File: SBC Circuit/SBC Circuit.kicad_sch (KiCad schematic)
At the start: 22 parts, among them J3 Conn_01x06_Pin, SW1 RESET, U1 MC68000FN, U11 MC34064P, U2 XC9572XL, X1 SG-531

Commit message: Wire phase done
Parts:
- added TP7: ~{BERR}, TestPoint:TestPoint_Keystone_5000-5004_Miniature, symbol Connector:TestPoint
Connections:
- net as: now also U2.28 (P28); no longer U2.22 (P22)
- net berr: now also U2.20 (P20), TP7.1; no longer U2.12 (P12)
- net dtack: now also U2.24 (P24); no longer U2.14 (P14)
- net fc0: now also U2.18 (P18); no longer U2.27 (P27)
- net fc1: now also U2.12 (P12); no longer U2.28 (P28)
- net fc2: now also U2.14 (P14); no longer U2.25 (P25)
- net ipl0: now also U2.13 (P13); no longer U2.26 (P26)
- net ipl1: now also U2.19 (P19); no longer U2.24 (P24)
- net ipl2: now also U2.22 (P22); no longer U2.13 (P13)
- net lds: now also U2.26 (P26); no longer U2.18 (P18)
- net rw: now also U2.25 (P25); no longer U2.19 (P19)
- net uds: now also U2.27 (P27); no longer U2.20 (P20)

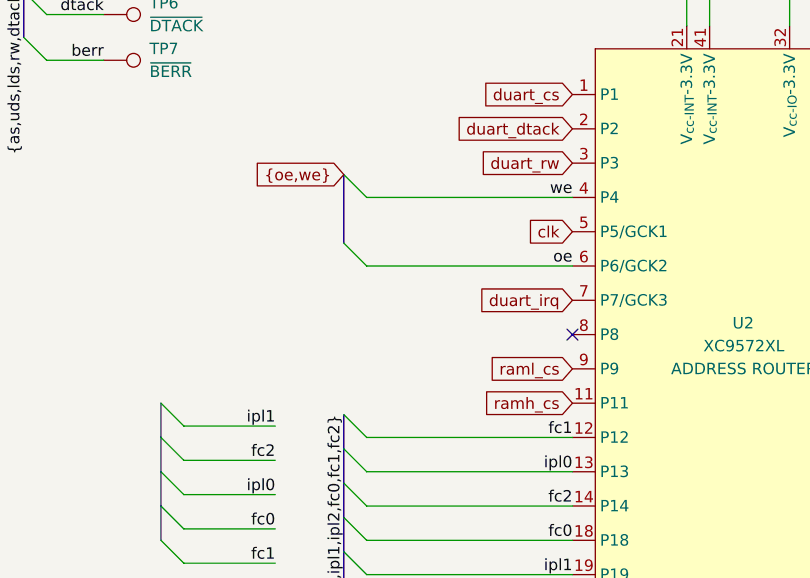
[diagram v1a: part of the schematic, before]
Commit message: Connect some power lines
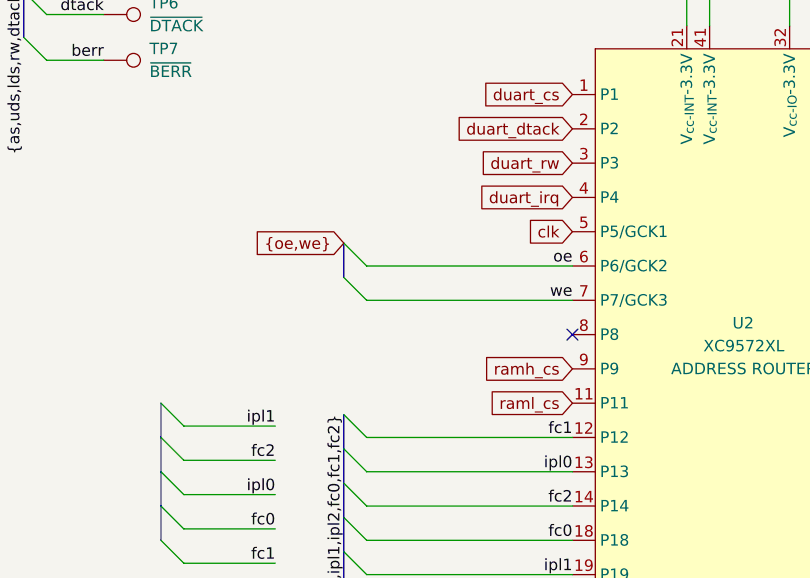
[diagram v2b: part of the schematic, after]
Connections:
- net duart_irq: now also U2.4 (P4); no longer U2.7 (P7/GCK3)
- net ramh_cs: now also U2.9 (P9); no longer U2.11 (P11)
- net raml_cs: now also U2.11 (P11); no longer U2.9 (P9)
- net we: now also U2.7 (P7/GCK3); no longer U2.4 (P4)
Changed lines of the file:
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@@
+    (stroke (width 0) (type default))
+  )
+  (bus_entry (at 58.42 128.27) (size 2.54 2.54)
     (stroke (width 0) (type default))
   )
@@
     (stroke (width 0) (type default))
   )
-  (bus_entry (at 58.42 120.65) (size 2.54 2.54)
+  (bus_entry (at 58.42 132.08) (size 2.54 2.54)
     (stroke (width 0) (type default))
   )
@@
     (stroke (width 0) (type default))
   )
-  (bus_entry (at 58.42 128.27) (size 2.54 2.54)
-    (stroke (width 0) (type default))
-  )
   (bus_entry (at 134.62 151.13) (size -2.54 2.54)
     (stroke (width 0) (type default))
@@
     (stroke (width 0) (type default))
   )
+  (wire (pts (xy 60.96 130.81) (xy 83.82 130.81))
+    (stroke (width 0) (type default))
+  )
   (wire (pts (xy 121.92 111.76) (xy 132.08 111.76))
     (stroke (width 0) (type default))
@@
     (stroke (width 0) (type default))
   )
+  (bus (pts (xy 58.42 128.27) (xy 58.42 132.08))
+    (stroke (width 0) (type default))
+  )
   (wire (pts (xy 106.68 55.88) (xy 106.68 50.8))
     (stroke (width 0) (type default))
@@
     (stroke (width 0) (type default))
   )
-  (wire (pts (xy 60.96 130.81) (xy 83.82 130.81))
-    (stroke (width 0) (type default))
-  )
   (wire (pts (xy 209.55 30.48) (xy 213.36 30.48))
     (stroke (width 0) (type default))
@@
     (stroke (width 0) (type default))
   )
-  (wire (pts (xy 60.96 123.19) (xy 83.82 123.19))
-    (stroke (width 0) (type default))
-  )
   (wire (pts (xy 93.98 38.1) (xy 93.98 41.91))
     (stroke (width 0) (type default))
@@
     (stroke (width 0) (type default))
   )
-  (bus (pts (xy 58.42 120.65) (xy 58.42 128.27))
-    (stroke (width 0) (type default))
-  )
   (bus (pts (xy 134.62 113.03) (xy 134.62 116.84))
     (stroke (width 0) (type default))
@@
   )
   (bus (pts (xy 264.16 53.34) (xy 264.16 55.88))
+    (stroke (width 0) (type default))
+  )
+  (wire (pts (xy 60.96 134.62) (xy 83.82 134.62))
     (stroke (width 0) (type default))
   )
@@
     (effects (font (size 1.27 1.27)) (justify left bottom))
   )
+  (label "fc1" (at 83.82 149.86 180)
+    (effects (font (size 1.27 1.27)) (justify right bottom))
+  )
+  (label "addr19" (at 251.46 96.52 0) (fields_autoplaced)
+    (effects (font (size 1.27 1.27)) (justify left bottom))
+  )
+  (label "fc1" (at 50.8 163.83 180) (fields_autoplaced)
+    (effects (font (size 1.27 1.27)) (justify right bottom))
+  )
+  (label "dtack" (at 200.66 77.47 180) (fields_autoplaced)
+    (effects (font (size 1.27 1.27)) (justify right bottom))
+  )
   (label "oe" (at 83.82 130.81 180) (fields_autoplaced)
-    (effects (font (size 1.27 1.27)) (justify right bottom))
-  )
-  (label "fc1" (at 83.82 149.86 180)
-    (effects (font (size 1.27 1.27)) (justify right bottom))
-  )
-  (label "addr19" (at 251.46 96.52 0) (fields_autoplaced)
-    (effects (font (size 1.27 1.27)) (justify left bottom))
-  )
-  (label "fc1" (at 50.8 163.83 180) (fields_autoplaced)
-    (effects (font (size 1.27 1.27)) (justify right bottom))
-  )
-  (label "dtack" (at 200.66 77.47 180) (fields_autoplaced)
     (effects (font (size 1.27 1.27)) (justify right bottom))
   )
@@
     (effects (font (size 1.27 1.27)) (justify left bottom))
   )
-  (label "we" (at 83.82 123.19 180) (fields_autoplaced)
-    (effects (font (size 1.27 1.27)) (justify right bottom))
-  )
   (label "{ipl0,ipl1,ipl2,fc0,fc1,fc2}" (at 187.96 91.44 180) (fields_autoplaced)
     (effects (font (size 1.27 1.27)) (justify right bottom))
@@
   (label "addr9" (at 251.46 71.12 0) (fields_autoplaced)
     (effects (font (size 1.27 1.27)) (justify left bottom))
+  )
+  (label "we" (at 83.82 134.62 180) (fields_autoplaced)
+    (effects (font (size 1.27 1.27)) (justify right bottom))
   )
   (label "data12" (at 251.46 139.7 0) (fields_autoplaced)
@@
     )
   )
-  (global_label "ramh_cs" (shape input) (at 83.82 146.05 180) (fields_autoplaced)
-    (effects (font (size 1.27 1.27)) (justify right))
-    (property "Intersheetrefs" "${INTERSHEET_REFS}" (at 72.973 146.05 0)
-      (effects (font (size 1.27 1.27)) (justify right) hide)
-    )
-    (property "Netclass" "signal" (at 83.82 148.2408 0)
-      (effects (font (size 1.27 1.27)) (justify right) hide)
-    )
-  )
-  (global_label "duart_irq" (shape input) (at 83.82 134.62 180) (fields_autoplaced)
-    (effects (font (size 1.27 1.27)) (justify right))
-    (property "Intersheetrefs" "${INTERSHEET_REFS}" (at 72.3683 134.62 0)
-      (effects (font (size 1.27 1.27)) (justify right) hide)
-    )
-    (property "Netclass" "signal" (at 83.82 136.8108 0)
-      (effects (font (size 1.27 1.27)) (justify right) hide)
-    )
-  )
-  (global_label "raml_cs" (shape input) (at 83.82 142.24 180) (fields_autoplaced)
-    (effects (font (size 1.27 1.27)) (justify right))
-    (property "Intersheetrefs" "${INTERSHEET_REFS}" (at 73.4568 142.24 0)
-      (effects (font (size 1.27 1.27)) (justify right) hide)
-    )
-    (property "Netclass" "signal" (at 83.82 144.4308 0)
-      (effects (font (size 1.27 1.27)) (justify right) hide)
-    )
-  )
   (global_label "clk" (shape input) (at 83.82 127 180) (fields_autoplaced)
     (effects (font (size 1.27 1.27)) (justify right))
@@
     )
   )
-  (global_label "{oe,we}" (shape input) (at 58.42 120.65 180) (fields_autoplaced)
+  (global_label "ramh_cs" (shape input) (at 83.82 142.24 180) (fields_autoplaced)
     (effects (font (size 1.27 1.27)) (justify right))
-    (property "Intersheetrefs" "${INTERSHEET_REFS}" (at 48.4799 120.65 0)
-      (effects (font (size 1.27 1.27)) (justify right) hide)
-    )
-    (property "Netclass" "bus" (at 58.42 122.8408 0)
+    (property "Intersheetrefs" "${INTERSHEET_REFS}" (at 72.973 142.24 0)
+      (effects (font (size 1.27 1.27)) (justify right) hide)
+    )
+    (property "Netclass" "signal" (at 83.82 144.4308 0)
+      (effects (font (size 1.27 1.27)) (justify right) hide)
+    )
+  )
+  (global_label "duart_irq" (shape input) (at 83.82 123.19 180) (fields_autoplaced)
+    (effects (font (size 1.27 1.27)) (justify right))
+    (property "Intersheetrefs" "${INTERSHEET_REFS}" (at 72.3683 123.19 0)
+      (effects (font (size 1.27 1.27)) (justify right) hide)
+    )
+    (property "Netclass" "signal" (at 83.82 125.3808 0)
+      (effects (font (size 1.27 1.27)) (justify right) hide)
+    )
+  )
+  (global_label "raml_cs" (shape input) (at 83.82 146.05 180) (fields_autoplaced)
+    (effects (font (size 1.27 1.27)) (justify right))
+    (property "Intersheetrefs" "${INTERSHEET_REFS}" (at 73.4568 146.05 0)
+      (effects (font (size 1.27 1.27)) (justify right) hide)
+    )
+    (property "Netclass" "signal" (at 83.82 148.2408 0)
       (effects (font (size 1.27 1.27)) (justify right) hide)
     )
@@
       (effects (font (size 1.27 1.27)) (justify right) hide)
     )
+  )
+  (global_label "{oe,we}" (shape input) (at 58.42 128.27 180) (fields_autoplaced)
+    (effects (font (size 1.27 1.27)) (justify right))
+    (property "Intersheetrefs" "${INTERSHEET_REFS}" (at 48.4799 128.27 0)
+      (effects (font (size 1.27 1.27)) (justify right) hide)
+    )
+    (property "Netclass" "bus" (at 58.42 130.4608 0)
+      (effects (font (size 1.27 1.27)) (justify right) hide)
+    )

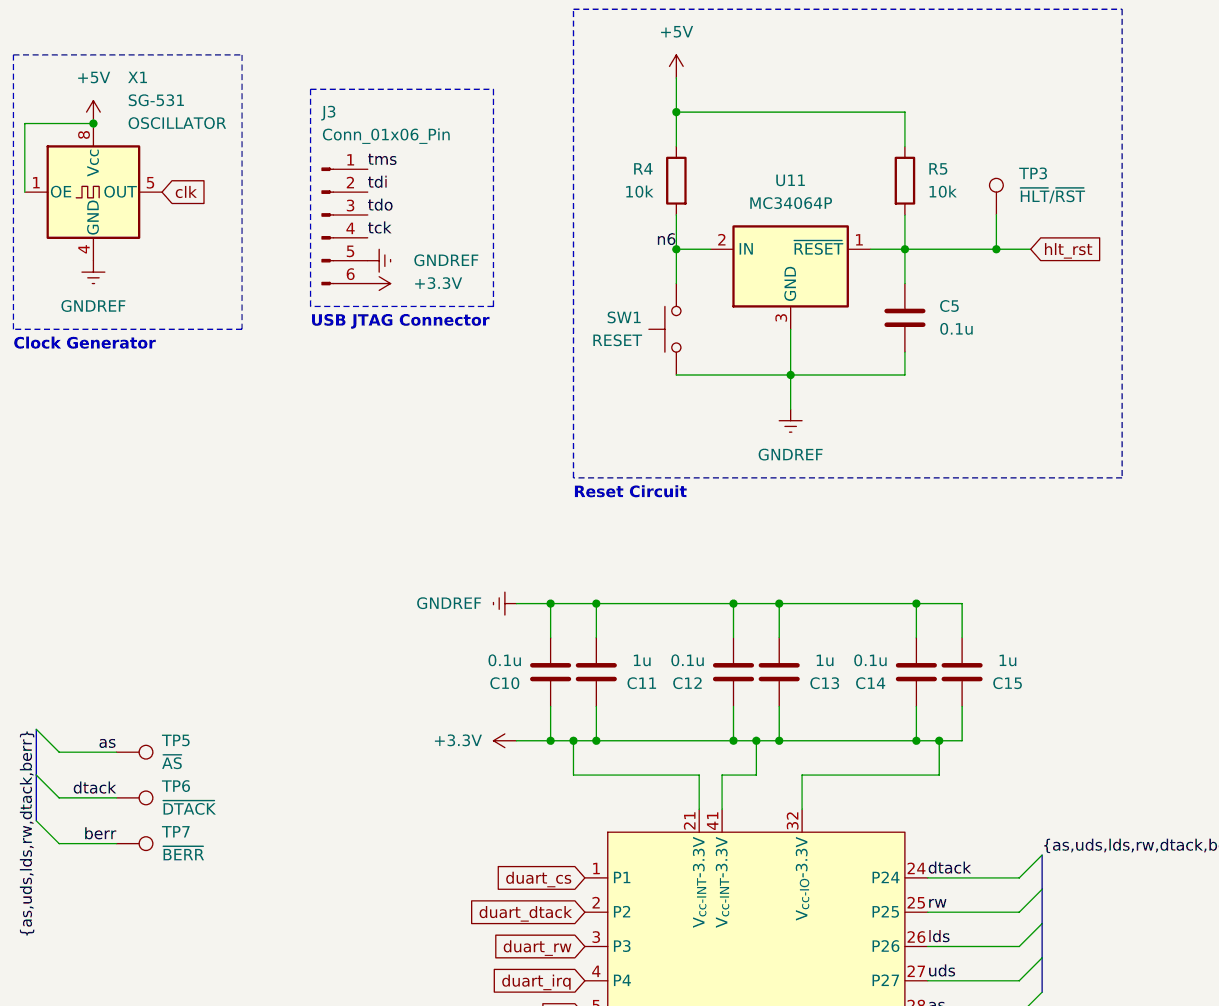
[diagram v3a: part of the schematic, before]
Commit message: Add ground test point
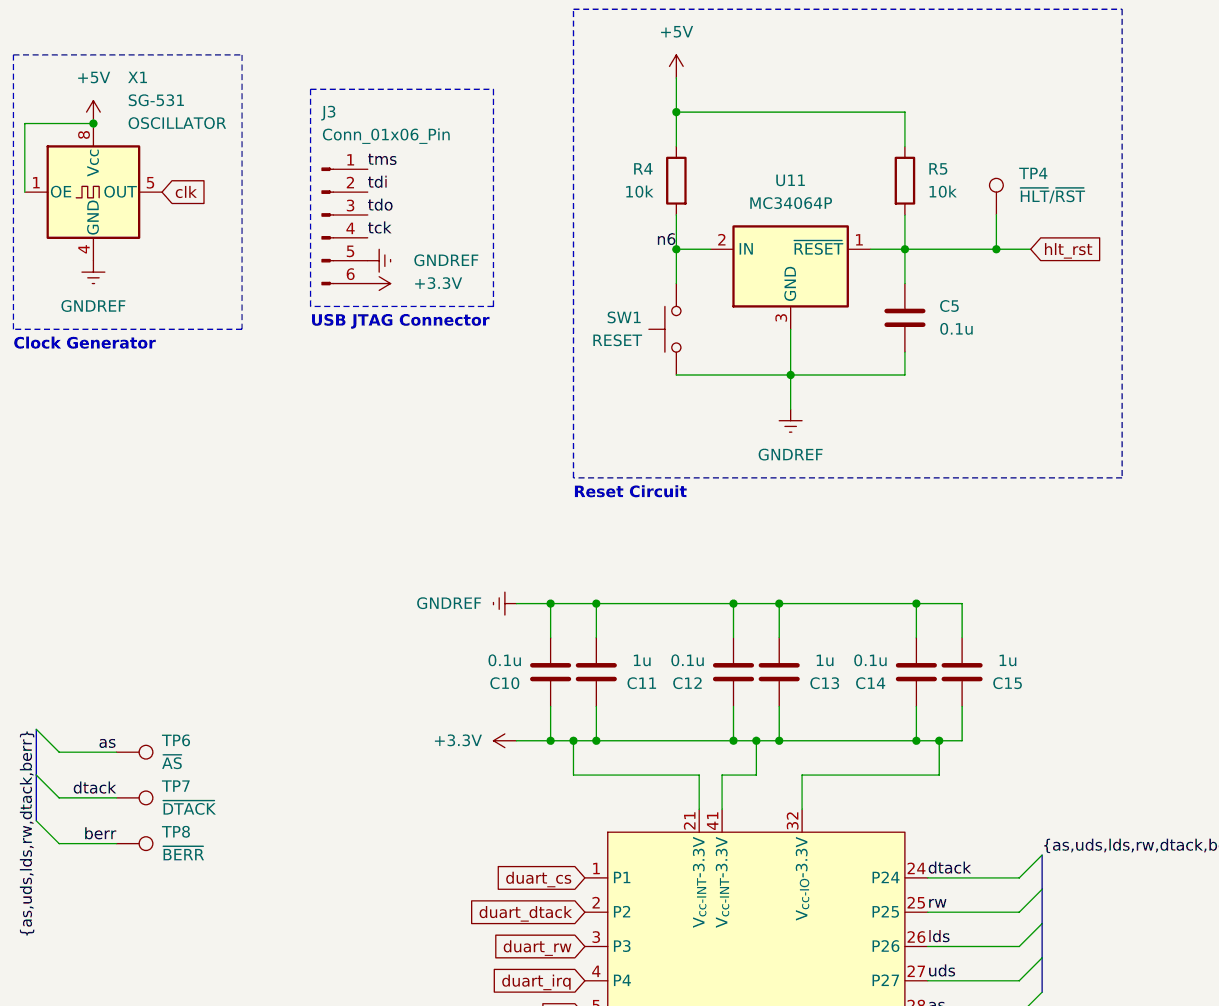
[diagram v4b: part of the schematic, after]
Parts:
- renumbered TP3 to TP4, TP5 to TP6, TP6 to TP7, TP7 to TP8
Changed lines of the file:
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@@
   (symbol (lib_id "Connector:TestPoint") (at 31.75 102.87 270) (unit 1)
     (in_bom yes) (on_board yes) (dnp no) (fields_autoplaced)
-    (property "Reference" "TP6" (at 36.83 101.6 90)
+    (property "Reference" "TP7" (at 36.83 101.6 90)
       (effects (font (size 1.27 1.27)) (justify left))
     )
@@
       (project "SBC Circuit"
         (path "/3db026c4-f98d-4c94-ab2a-d9924b8daebe"
-          (reference "TP6") (unit 1)
+          (reference "TP7") (unit 1)
         )
       )
@@
   (symbol (lib_id "Connector:TestPoint") (at 31.75 97.79 270) (unit 1)
     (in_bom yes) (on_board yes) (dnp no) (fields_autoplaced)
-    (property "Reference" "TP5" (at 36.83 96.52 90)
+    (property "Reference" "TP6" (at 36.83 96.52 90)
       (effects (font (size 1.27 1.27)) (justify left))
     )
@@
       (project "SBC Circuit"
         (path "/3db026c4-f98d-4c94-ab2a-d9924b8daebe"
-          (reference "TP5") (unit 1)
+          (reference "TP6") (unit 1)
         )
       )
@@
   (symbol (lib_id "Connector:TestPoint") (at 129.54 38.1 0) (unit 1)
     (in_bom yes) (on_board yes) (dnp no) (fields_autoplaced)
-    (property "Reference" "TP3" (at 132.08 33.528 0)
+    (property "Reference" "TP4" (at 132.08 33.528 0)
       (effects (font (size 1.27 1.27)) (justify left))
     )
@@
       (project "SBC Circuit"
         (path "/3db026c4-f98d-4c94-ab2a-d9924b8daebe"
-          (reference "TP3") (unit 1)
+          (reference "TP4") (unit 1)
         )
       )
@@
   (symbol (lib_id "Connector:TestPoint") (at 31.75 107.95 270) (unit 1)
     (in_bom yes) (on_board yes) (dnp no) (fields_autoplaced)
-    (property "Reference" "TP7" (at 36.83 106.68 90)
+    (property "Reference" "TP8" (at 36.83 106.68 90)
       (effects (font (size 1.27 1.27)) (justify left))
     )
@@
       (project "SBC Circuit"
         (path "/3db026c4-f98d-4c94-ab2a-d9924b8daebe"
-          (reference "TP7") (unit 1)
-        )
-      )
+          (reference "TP8") (unit 1)
+        )
+      )

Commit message: Update schematic and PCB for requested changes
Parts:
- added C6: 0.1u, Capacitor_THT:CP_Disc_L5.50mm_W4.00mm_P2.50mm_NonPolarized, symbol Device:C
- added C7: 1u, Capacitor_THT:CP_Disc_L5.50mm_W4.00mm_P2.50mm_NonPolarized, symbol Device:C
- added R13, R6: 10k, Resistor_THT:R_Axial_DIN0204_L3.6mm_D1.6mm_P2.54mm_Vertical, symbol Device:R
- TP4: value ~{HLT}/~{RST} -> ~{RST}
- renumbered C6 to C10, C7 to C11, C8 to C12, C9 to C13, C10 to C14, C11 to C15, C12 to C16, C13 to C17, C14 to C18, C15 to C19
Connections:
- net +3.3V: now also R13.1
- net +5V: now also C6.1, C7.1
- net GNDREF: now also C6.2, C7.2, R6.2; no longer SW1.2
- net berr: now also U2.18 (P18); no longer U2.20 (P20)
- net fc0: now also U2.19 (P19); no longer U2.18 (P18)
- net fc1: now also U2.11 (P11); no longer U2.12 (P12)
- net fc2: now also U2.13 (P13); no longer U2.14 (P14)
- net ipl0: now also U2.12 (P12); no longer U2.13 (P13)
- net ipl1: now also U2.14 (P14); no longer U2.19 (P19)
- net ipl2: now also U2.20 (P20); no longer U2.22 (P22)
- net ramh_cs: now also U2.8 (P8); no longer U2.9 (P9)
- net raml_cs: now also U2.9 (P9); no longer U2.11 (P11)
- net hlt_rst renamed rst
- net rst: no longer U1.19 (~{HALT})
- new net hlt: R13.2, U1.19 (~{HALT}), U2.22 (P22)
- new net n10: R6.1, SW1.2
- no-connect marks 4 -> 3
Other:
- moved on the sheet: J3, X1
